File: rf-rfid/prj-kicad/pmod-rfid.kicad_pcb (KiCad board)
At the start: 2 copper layers, 38.1 x 20.3 mm, 1 part, among them P1 PMOD

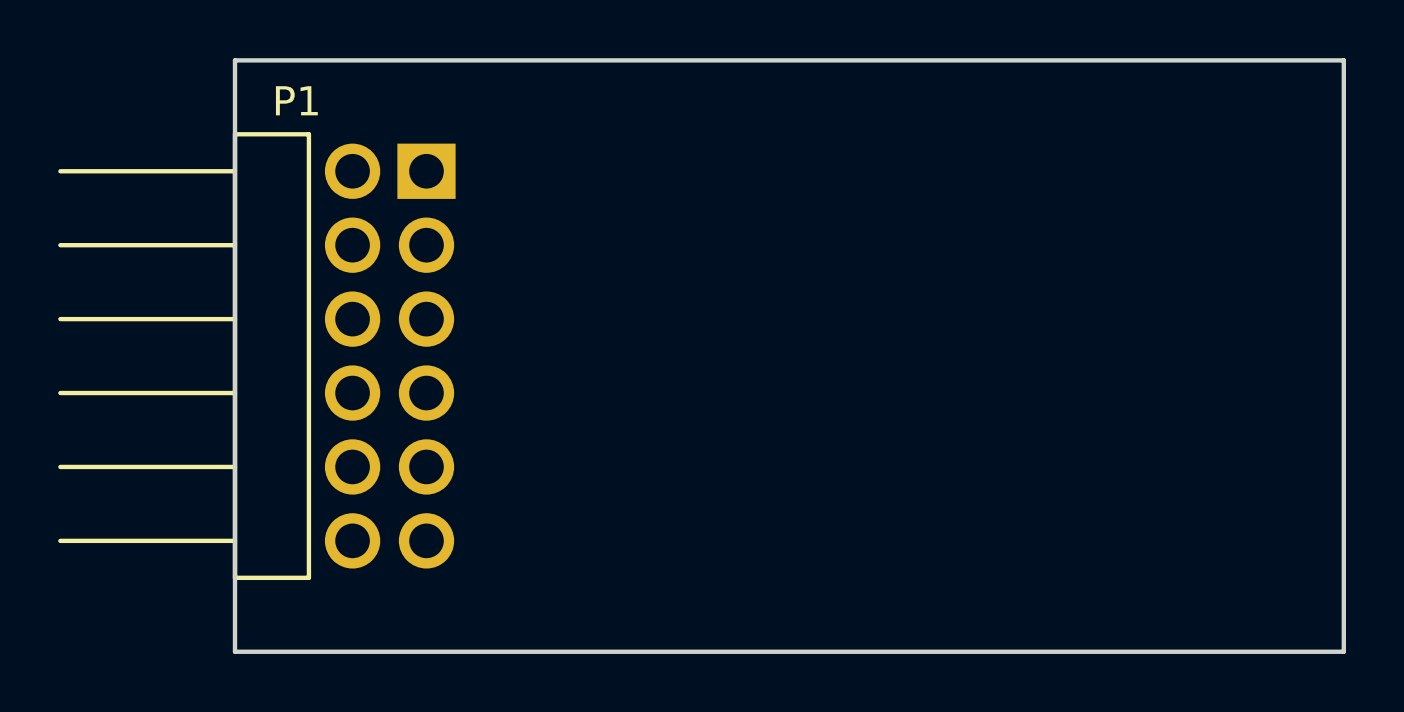
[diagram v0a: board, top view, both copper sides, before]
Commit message: RF-RFID: Update board routing
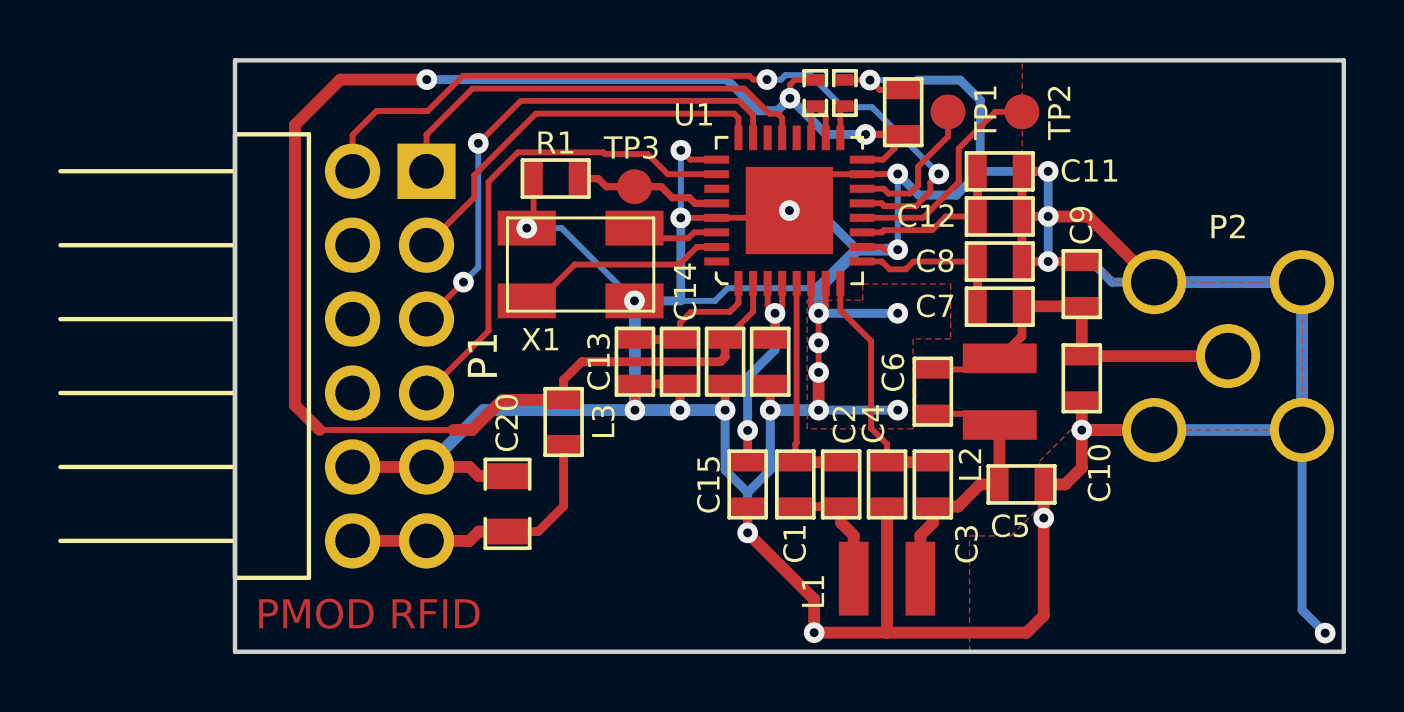
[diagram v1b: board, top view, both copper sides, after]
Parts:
- added C1: 1,5nF, pmod-rfid:SMD0603, F.Cu at (148.7, 109.4)
- added C10: 27pF, pmod-rfid:SMD0603, F.Cu at (158.5, 105.8)
- added C11: 2,2uF, pmod-rfid:SMD0603, F.Cu at (155.7, 98.7)
- added C12: 10nF, pmod-rfid:SMD0603, F.Cu at (155.7, 100.2)
- added C13: 2,2uF, pmod-rfid:SMD0603, F.Cu at (143.2, 105.2)
- added C14: 10nF, pmod-rfid:SMD0603, F.Cu at (144.7, 105.2)
- added C15: 2,2uF, pmod-rfid:SMD0603, F.Cu at (147.1, 109.4)
- added C16: 10nF, pmod-rfid:SMD0603, F.Cu at (147.8, 105.2)
- added C18: 100nF, pmod-rfid:SMD0603, F.Cu at (152.4, 96.6)
- added C19: 100nF, pmod-rfid:SMD0603, F.Cu at (146.3, 105.2)
- added C2: 1,5nF, pmod-rfid:SMD0603, F.Cu at (150.3, 109.4)
- added C20: C, pmod-rfid:SMD0805, F.Cu at (138.8, 110.1)
- added C3: 1,2nF, pmod-rfid:SMD0603, F.Cu at (153.4, 109.4)
- added C4: 1,2nF, pmod-rfid:SMD0603, F.Cu at (151.9, 109.4)
- added C5: 680pF, pmod-rfid:SMD0603, F.Cu at (156.5, 109.4)
- added C6: 10pF, pmod-rfid:SMD0603, F.Cu at (153.4, 106.2)
- added C7: 220pF, pmod-rfid:SMD0603, F.Cu at (155.7, 103.3)
- added C8: 680pF, pmod-rfid:SMD0603, F.Cu at (155.7, 101.8)
- added C9: 100pF, pmod-rfid:SMD0603, F.Cu at (158.5, 102.5)
- added L1: INDUCTOR, pmod-rfid:I_1008CS, F.Cu at (151.9, 112.6)
- added L2: 330nH, pmod-rfid:I_1008CS, F.Cu at (155.7, 106.2)
- added L3: FB1000, pmod-rfid:SMD0603, F.Cu at (140.7, 107.3)
- added P2: ANTENNA, pmod-rfid:CONN_SMA_RA, F.Cu at (163.6, 105.0)
- added R1: 10k, pmod-rfid:SMD0603, F.Cu at (140.5, 98.9)
- added R2: 0, pmod-rfid:SMD0402, F.Cu at (150.4, 96.0)
- added R3: 0, pmod-rfid:SMD0402, F.Cu at (149.4, 96.0)
- added TP1: CONN_1, pmod-rfid:TP_SMD, F.Cu at (153.9, 96.6)
- added TP2: CONN_1, pmod-rfid:TP_SMD, F.Cu at (156.5, 96.6)
- added TP3: CONN_1, pmod-rfid:TP_SMD, F.Cu at (143.2, 99.2)
- added U1: TRF7970, pmod-rfid:QFN32, F.Cu at (148.5, 100.0)
- added X1: 13,56MHz, pmod-rfid:Q_SMD5x3, F.Cu at (141.3, 101.9)
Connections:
- P1 pad 1: (no net) -> SPI_NSS
- P1 pad 10: (no net) -> Net-(P1-Pad10)
- P1 pad 11: (no net) -> GND
- P1 pad 12: (no net) -> +3.3V
- P1 pad 2: (no net) -> SPI_MOSI
- P1 pad 3: (no net) -> SPI_MISO
- P1 pad 4: (no net) -> SPI_SCK
- P1 pad 5: (no net) -> GND
- P1 pad 6: (no net) -> +3.3V
- P1 pad 7: (no net) -> SPI_IT
- P1 pad 8: (no net) -> RESET
- P1 pad 9: (no net) -> Net-(P1-Pad9)
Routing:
- net GND: track 0.00 -> 171.1 mm, vias 0 -> 26
- net +Vrfid: track 0.00 -> 55.1 mm, vias 0 -> 3
- net SPI_IT: track 0.00 -> 27.1 mm, vias 0 -> 2
- net SPI_MISO: track 0.00 -> 17.8 mm, vias 0 -> 2
- net SPI_SCK: track 0.00 -> 16.7 mm
- net SPI_NSS: track 0.00 -> 15.2 mm
- net SPI_MOSI: track 0.00 -> 13.8 mm
- net Net-(C10-Pad1): track 0.00 -> 13.4 mm
- net +3.3V: track 0.00 -> 9.88 mm
- net Net-(C3-Pad1): track 0.00 -> 9.76 mm
- net Net-(C15-Pad1): track 0.00 -> 8.75 mm, vias 0 -> 2
- net Net-(C3-Pad2): track 0.00 -> 8.39 mm
- net Net-(C1-Pad2): track 0.00 -> 7.74 mm
- net Net-(TP2-Pad1): track 0.00 -> 7.67 mm
- net Net-(U1-Pad31): track 0.00 -> 7.29 mm
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- added copper zone on B.Cu, net GND
- added copper zone on F.Cu, net GND
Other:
- board text added: "PMOD RFID"

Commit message: RF-RFID: Update board silkscreen
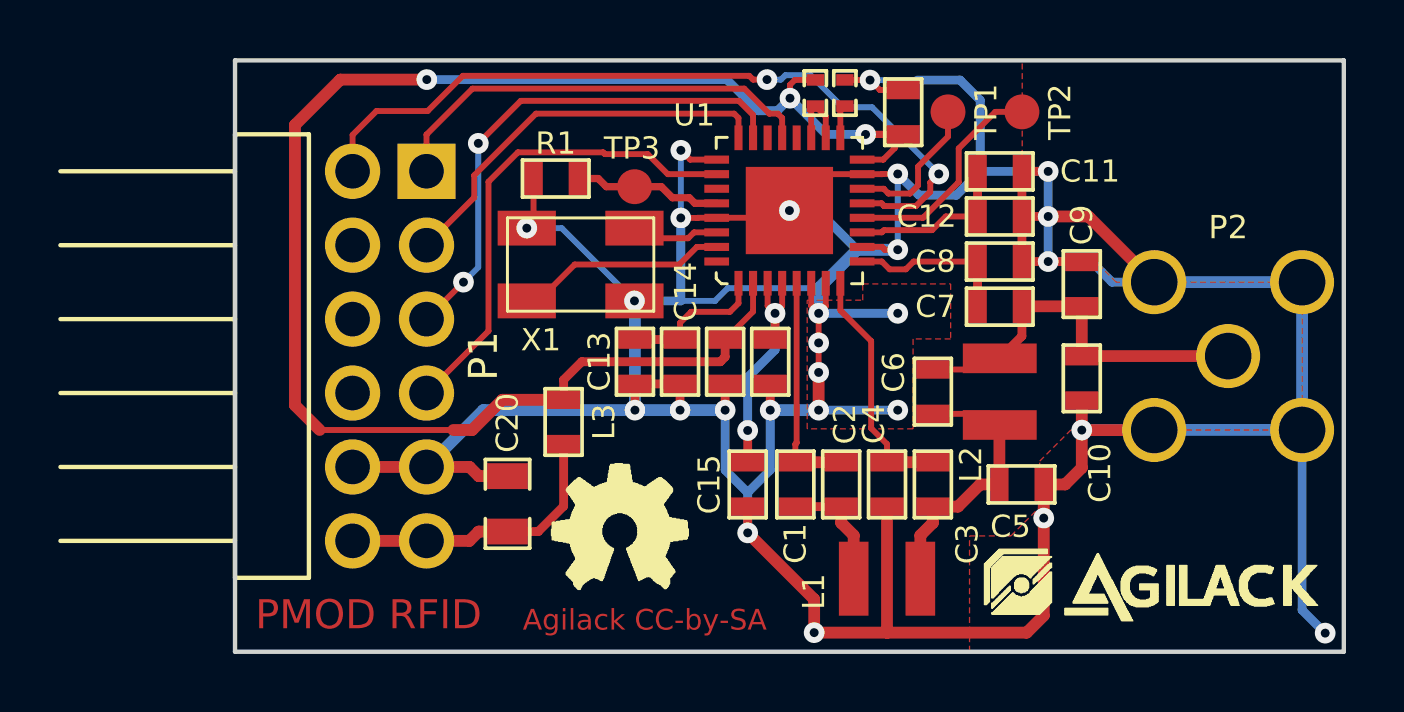
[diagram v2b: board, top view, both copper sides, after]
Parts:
- added agilack-11.5: 450px, pmod-rfid:logo-agilack-11.5, F.Cu at (161.3, 112.9)
- added ohw_logo: VAL**, pmod-rfid:logo-ohw, F.Cu at (142.7, 111.0)
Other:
- board text added: "Agilack CC-by-SA"
